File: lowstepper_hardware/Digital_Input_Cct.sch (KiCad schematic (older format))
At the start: 5 parts, among them J12 PJ398SM-12, Q1 MMBT3904

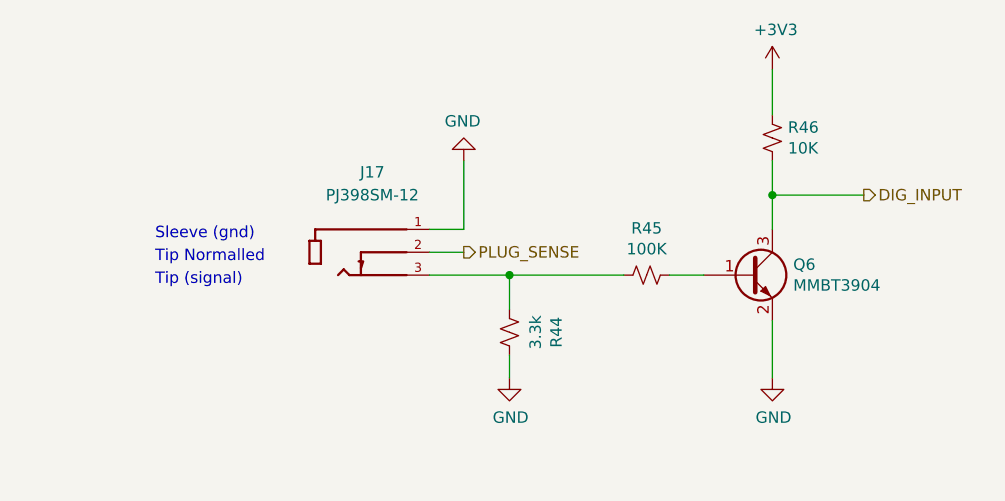
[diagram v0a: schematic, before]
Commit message: JLCPCB test & rename footprints
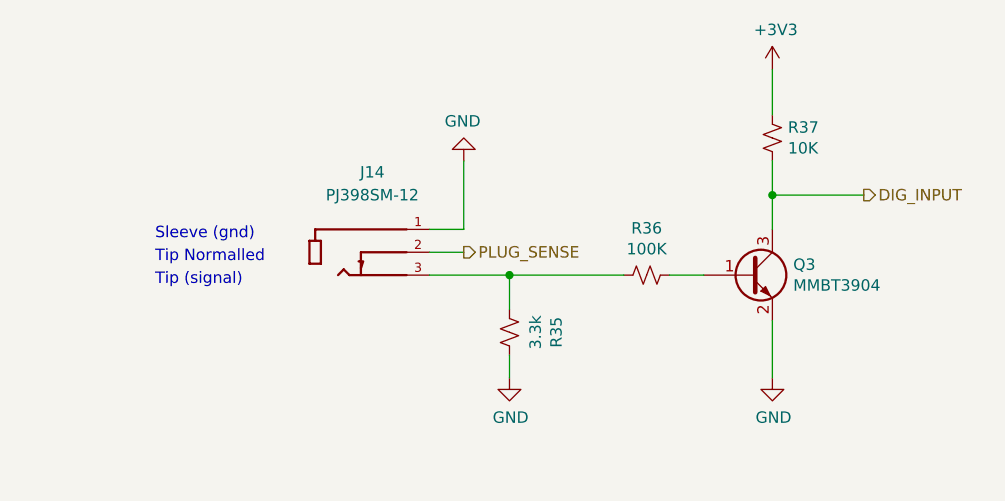
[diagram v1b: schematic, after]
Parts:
- Q1: footprint TO_SOT_Packages_SMD:SOT-23 -> Package_TO_SOT_SMD:SOT-23
- R1, R4, R7: footprint Resistors_SMD:R_0603_HandSoldering -> Resistor_SMD:R_0603_1608Metric_Pad0.98x0.95mm_HandSolder
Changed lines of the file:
@@
 $Descr A4 11693 8268
 encoding utf-8
-Sheet 8 13
+Sheet 10 13
 Title "Lowstepper"
 Date "2021-03-06"
@@
 AR Path="/604B0276/6045022C" Ref="Q5"  Part="1"
 AR Path="/604BE180/6045022C" Ref="Q6"  Part="1"
-F 0 "Q6" H 6591 3796 50  0000 L CNN
+F 0 "Q3" H 6591 3796 50  0000 L CNN
 F 1 "MMBT3904" H 6591 3705 50  0000 L CNN
-F 2 "TO_SOT_Packages_SMD:SOT-23" H 6600 3675 50  0001 L CIN
+F 2 "Package_TO_SOT_SMD:SOT-23" H 6600 3675 50  0001 L CIN
 F 3 "https://www.fairchildsemi.com/datasheets/2N/2N3904.pdf" H 6400 3750 50  0001 L CNN
 	1    6400 3750
@@
 AR Path="/604B0276/60450238" Ref="R42"  Part="1"
 AR Path="/604BE180/60450238" Ref="R45"  Part="1"
-F 0 "R45" V 5745 3750 50  0000 C CNN
+F 0 "R36" V 5745 3750 50  0000 C CNN
 F 1 "100K" V 5836 3750 50  0000 C CNN
-F 2 "Resistors_SMD:R_0603_HandSoldering" H 5950 3750 50  0001 C CNN
+F 2 "Resistor_SMD:R_0603_1608Metric_Pad0.98x0.95mm_HandSolder" H 5950 3750 50  0001 C CNN
 F 3 "~" H 5950 3750 50  0001 C CNN
 	1    5950 3750
@@
 AR Path="/604B0276/60450244" Ref="R43"  Part="1"
 AR Path="/604BE180/60450244" Ref="R46"  Part="1"
-F 0 "R46" H 6432 3104 50  0000 R CNN
+F 0 "R37" H 6432 3104 50  0000 R CNN
 F 1 "10K" H 6432 3195 50  0000 R CNN
-F 2 "Resistors_SMD:R_0603_HandSoldering" H 6500 3150 50  0001 C CNN
+F 2 "Resistor_SMD:R_0603_1608Metric_Pad0.98x0.95mm_HandSolder" H 6500 3150 50  0001 C CNN
 F 3 "~" H 6500 3150 50  0001 C CNN
 	1    6500 3150
@@
 AR Path="/604B0276/60450260" Ref="J16"  Part="1"
 AR Path="/604BE180/60450260" Ref="J17"  Part="1"
-F 0 "J17" H 4750 3800 50  0000 C CNN
+F 0 "J14" H 4750 3800 50  0000 C CNN
 F 1 "PJ398SM-12" H 4750 3700 50  0000 C CNN
 F 2 "THONK_PJ398SM-12" H 4700 3550 50  0001 L BNN
@@
 AR Path="/604B0276/60450267" Ref="R41"  Part="1"
 AR Path="/604BE180/60450267" Ref="R44"  Part="1"
-F 0 "R44" V 5145 4000 50  0000 C CNN
+F 0 "R35" V 5145 4000 50  0000 C CNN
 F 1 "3.3k" V 5236 4000 50  0000 C CNN
-F 2 "Resistors_SMD:R_0603_HandSoldering" H 5350 4000 50  0001 C CNN
+F 2 "Resistor_SMD:R_0603_1608Metric_Pad0.98x0.95mm_HandSolder" H 5350 4000 50  0001 C CNN
 F 3 "~" H 5350 4000 50  0001 C CNN
 	1    5350 4000

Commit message: halfway through the sandwich...
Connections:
- net DIG_INPUT_BOTTOM: now reaches R1.2, R4.2
- net DIG_INPUT_BOTTOM: no longer J12.3
- new net DIG_INPUT_TOP: J12.3
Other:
- moved on the sheet: J14

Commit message: cu pours
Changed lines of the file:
@@
 $Descr A4 11693 8268
 encoding utf-8
-Sheet 9 13
+Sheet 13 13
 Title "Lowstepper"
 Date "2021-03-06"
@@
 AR Path="/604B0276/60450267" Ref="R41"  Part="1"
 AR Path="/604BE180/60450267" Ref="R44"  Part="1"
-F 0 "R35" V 5145 4000 50  0000 C CNN
+F 0 "R32" V 5145 4000 50  0000 C CNN
 F 1 "3.3k" V 5236 4000 50  0000 C CNN
 F 2 "Resistor_SMD:R_0603_1608Metric_Pad0.98x0.95mm_HandSolder" H 5350 4000 50  0001 C CNN
@@
 AR Path="/604B0276/60450244" Ref="R43"  Part="1"
 AR Path="/604BE180/60450244" Ref="R46"  Part="1"
-F 0 "R37" H 6432 3104 50  0000 R CNN
+F 0 "R34" H 6432 3104 50  0000 R CNN
 F 1 "10K" H 6432 3195 50  0000 R CNN
 F 2 "Resistor_SMD:R_0603_1608Metric_Pad0.98x0.95mm_HandSolder" H 6500 3150 50  0001 C CNN
@@
 AR Path="/604B0276/60450238" Ref="R42"  Part="1"
 AR Path="/604BE180/60450238" Ref="R45"  Part="1"
-F 0 "R36" V 5745 3750 50  0000 C CNN
+F 0 "R33" V 5745 3750 50  0000 C CNN
 F 1 "100K" V 5836 3750 50  0000 C CNN
 F 2 "Resistor_SMD:R_0603_1608Metric_Pad0.98x0.95mm_HandSolder" H 5950 3750 50  0001 C CNN
@@
 AR Path="/604B0276/6045022C" Ref="Q5"  Part="1"
 AR Path="/604BE180/6045022C" Ref="Q6"  Part="1"
-F 0 "Q3" H 6591 3796 50  0000 L CNN
+F 0 "Q2" H 6591 3796 50  0000 L CNN
 F 1 "MMBT3904" H 6591 3705 50  0000 L CNN
 F 2 "Package_TO_SOT_SMD:SOT-23" H 6600 3675 50  0001 L CIN
@@
 AR Path="/604B0276/60450260" Ref="J16"  Part="1"
 AR Path="/604BE180/60450260" Ref="J17"  Part="1"
-F 0 "J14" H 4150 3800 50  0000 C CNN
+F 0 "J13" H 4150 3800 50  0000 C CNN
 F 1 "PJ398SM-12" H 4150 3700 50  0000 C CNN
 F 2 "THONK_PJ398SM-12" H 4100 3550 50  0001 L BNN

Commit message: dancers hw
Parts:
- R1, R4, R7: footprint Resistor_SMD:R_0603_1608Metric_Pad0.98x0.95mm_HandSolder -> Resistor_SMD:R_0402_1005Metric
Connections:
- net DIG_INPUT_TOP is gone; now on an unnamed net: J12.3
- net DIG_INPUT_BOTTOM: no longer names the net of R1.2, R4.2
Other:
- moved on the sheet: J13
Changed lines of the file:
@@
 $Descr A4 11693 8268
 encoding utf-8
-Sheet 13 13
+Sheet 5 8
 Title "Lowstepper"
 Date "2021-03-06"
@@
 F 0 "R32" V 5145 4000 50  0000 C CNN
 F 1 "3.3k" V 5236 4000 50  0000 C CNN
-F 2 "Resistor_SMD:R_0603_1608Metric_Pad0.98x0.95mm_HandSolder" H 5350 4000 50  0001 C CNN
+F 2 "Resistor_SMD:R_0402_1005Metric" H 5350 4000 50  0001 C CNN
 F 3 "~" H 5350 4000 50  0001 C CNN
 	1    5350 4000
@@
 F 0 "R34" H 6432 3104 50  0000 R CNN
 F 1 "10K" H 6432 3195 50  0000 R CNN
-F 2 "Resistor_SMD:R_0603_1608Metric_Pad0.98x0.95mm_HandSolder" H 6500 3150 50  0001 C CNN
+F 2 "Resistor_SMD:R_0402_1005Metric" H 6500 3150 50  0001 C CNN
 F 3 "~" H 6500 3150 50  0001 C CNN
 	1    6500 3150
@@
 Wire Wire Line
 	6500 3950 6500 4200
-$Comp
-L Device:R_Small_US R4
-U 1 1 60450238
-P 5950 3750
-AR Path="/6044C60B/60450238" Ref="R4"  Part="1"
-AR Path="/60488A39/60450238" Ref="R33"  Part="1"
-AR Path="/604956D4/60450238" Ref="R36"  Part="1"
-AR Path="/604A299D/60450238" Ref="R39"  Part="1"
-AR Path="/604B0276/60450238" Ref="R42"  Part="1"
-AR Path="/604BE180/60450238" Ref="R45"  Part="1"
-F 0 "R33" V 5745 3750 50  0000 C CNN
-F 1 "100K" V 5836 3750 50  0000 C CNN
-F 2 "Resistor_SMD:R_0603_1608Metric_Pad0.98x0.95mm_HandSolder" H 5950 3750 50  0001 C CNN
-F 3 "~" H 5950 3750 50  0001 C CNN
-	1    5950 3750
-	0    1    1    0
-$EndComp
 $Comp
 L power:GND #PWR0128
@@
 	1    0    0    -1
 $EndComp
-Text Notes 3200 3600 0    50   ~ 0
+Text Notes 3650 3600 0    50   ~ 0
 Sleeve (gnd)
-Text Notes 3200 3800 0    50   ~ 0
+Text Notes 3650 3800 0    50   ~ 0
 Tip (signal)
-Text Notes 3200 3700 0    50   ~ 0
+Text Notes 3650 3700 0    50   ~ 0
 Tip Normalled
-Wire Wire Line
-	4400 3750 4750 3750
-Wire Wire Line
-	4400 3550 4550 3550
-Wire Wire Line
-	4400 3650 4550 3650
-Text HLabel 4550 3650 2    50   Output ~ 0
-PLUG_SENSE
+Connection ~ 5350 3750
+$Comp
+L PJ398SM-12:PJ398SM-12 J12
+U 1 1 60450260
+P 4500 3550
+AR Path="/6044C60B/60450260" Ref="J12"  Part="1"
+AR Path="/60488A39/60450260" Ref="J13"  Part="1"
+AR Path="/604956D4/60450260" Ref="J14"  Part="1"
+AR Path="/604A299D/60450260" Ref="J15"  Part="1"
+AR Path="/604B0276/60450260" Ref="J16"  Part="1"
+AR Path="/604BE180/60450260" Ref="J17"  Part="1"
+F 0 "J13" H 4550 3800 50  0000 C CNN
+F 1 "PJ398SM-12" H 4550 3700 50  0000 C CNN
+F 2 "THONK_PJ398SM-12" H 4500 3550 50  0001 L BNN
+F 3 "" H 4500 3550 50  0001 L BNN
+F 4 "14.5 mm" H 4500 3550 50  0001 L BNN "MAXIMUM_PACKAGE_HEIGHT"
+F 5 "Thonk" H 4500 3550 50  0001 L BNN "MANUFACTURER"
+F 6 "1" H 4500 3550 50  0001 L BNN "PARTREV"
+F 7 "Manufacturer Recommendations" H 4500 3550 50  0001 L BNN "STANDARD"
+	1    4500 3550
+	1    0    0    -1
+$EndComp
+Wire Wire Line
+	4950 3550 4950 3250
 $Comp
 L power:GND #PWR0130
 U 1 1 60450250
-P 4550 3250
+P 4950 3250
 AR Path="/6044C60B/60450250" Ref="#PWR0130"  Part="1"
 AR Path="/60488A39/60450250" Ref="#PWR0149"  Part="1"
@@
 AR Path="/604B0276/60450250" Ref="#PWR0161"  Part="1"
 AR Path="/604BE180/60450250" Ref="#PWR0165"  Part="1"
-F 0 "#PWR0149" H 4550 3000 50  0001 C CNN
-F 1 "GND" H 4555 3077 50  0000 C CNN
-F 2 "" H 4550 3250 50  0001 C CNN
-F 3 "" H 4550 3250 50  0001 C CNN
-	1    4550 3250
+F 0 "#PWR0149" H 4950 3000 50  0001 C CNN
+F 1 "GND" H 4955 3077 50  0000 C CNN
+F 2 "" H 4950 3250 50  0001 C CNN
+F 3 "" H 4950 3250 50  0001 C CNN
+	1    4950 3250
 	-1   0    0    1
 $EndComp
-Wire Wire Line
-	4550 3550 4550 3250
-$Comp
-L PJ398SM-12:PJ398SM-12 J12
-U 1 1 60450260
-P 4100 3550
-AR Path="/6044C60B/60450260" Ref="J12"  Part="1"
-AR Path="/60488A39/60450260" Ref="J13"  Part="1"
-AR Path="/604956D4/60450260" Ref="J14"  Part="1"
-AR Path="/604A299D/60450260" Ref="J15"  Part="1"
-AR Path="/604B0276/60450260" Ref="J16"  Part="1"
-AR Path="/604BE180/60450260" Ref="J17"  Part="1"
-F 0 "J13" H 4150 3800 50  0000 C CNN
-F 1 "PJ398SM-12" H 4150 3700 50  0000 C CNN
-F 2 "THONK_PJ398SM-12" H 4100 3550 50  0001 L BNN
-F 3 "" H 4100 3550 50  0001 L BNN
-F 4 "14.5 mm" H 4100 3550 50  0001 L BNN "MAXIMUM_PACKAGE_HEIGHT"
-F 5 "Thonk" H 4100 3550 50  0001 L BNN "MANUFACTURER"
-F 6 "1" H 4100 3550 50  0001 L BNN "PARTREV"
-F 7 "Manufacturer Recommendations" H 4100 3550 50  0001 L BNN "STANDARD"
-	1    4100 3550
-	1    0    0    -1
-$EndComp
-Text HLabel 4750 3750 3    50   Input ~ 0
-DIG_INPUT_TOP
-Wire Wire Line
-	5350 3750 5150 3750
-Connection ~ 5350 3750
-Text HLabel 5150 3750 3    50   Input ~ 0
-DIG_INPUT_BOTTOM
+Text HLabel 4950 3650 2    50   Output ~ 0
+PLUG_SENSE
+Wire Wire Line
+	4800 3650 4950 3650
+Wire Wire Line
+	4800 3550 4950 3550
+Wire Wire Line
+	4800 3750 5350 3750
+$Comp
+L Device:R_Small_US R4
+U 1 1 60450238
+P 5950 3750
+AR Path="/6044C60B/60450238" Ref="R4"  Part="1"
+AR Path="/60488A39/60450238" Ref="R33"  Part="1"
+AR Path="/604956D4/60450238" Ref="R36"  Part="1"
+AR Path="/604A299D/60450238" Ref="R39"  Part="1"
+AR Path="/604B0276/60450238" Ref="R42"  Part="1"
+AR Path="/604BE180/60450238" Ref="R45"  Part="1"
+F 0 "R33" V 5745 3750 50  0000 C CNN
+F 1 "100K" V 5836 3750 50  0000 C CNN
+F 2 "Resistor_SMD:R_0402_1005Metric" H 5950 3750 50  0001 C CNN
+F 3 "~" H 5950 3750 50  0001 C CNN
+	1    5950 3750
+	0    1    1    0
+$EndComp
 $EndSCHEMATC
